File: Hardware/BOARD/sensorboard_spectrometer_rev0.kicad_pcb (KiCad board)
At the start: 2 copper layers, 69.1 x 54.9 mm, 41 parts, among them IC1 CAT4101, U10 ADS1115IDGS, U11 TPS61088RHLT, U3 LILTGO touch, U4 W25Q16JVSS, U5 TLV9001IDCK, U6 MCP9808_MSOP, U7 TRANSLATOR-TXS0108E, U8 DS3231MZ, U9 LT3045xDD

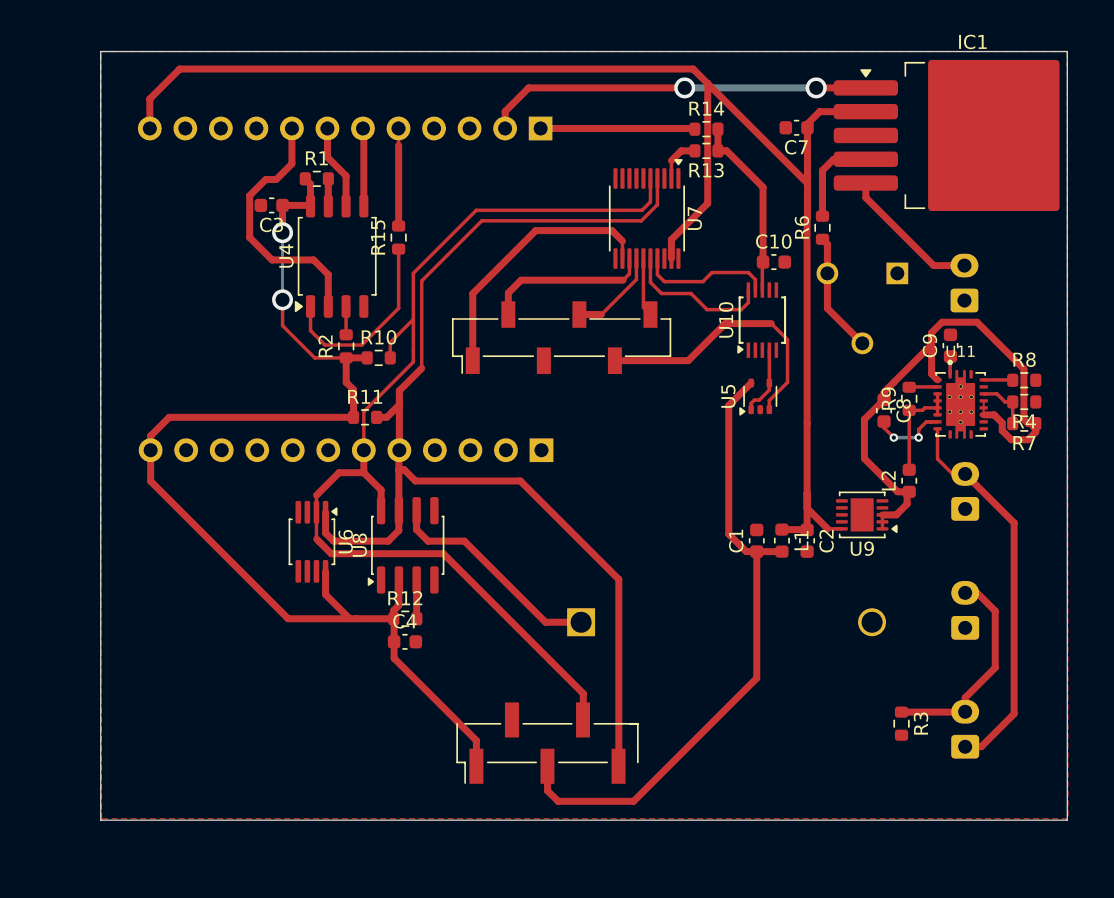
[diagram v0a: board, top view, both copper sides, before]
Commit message: new pcb with the as7331(uv sensor)
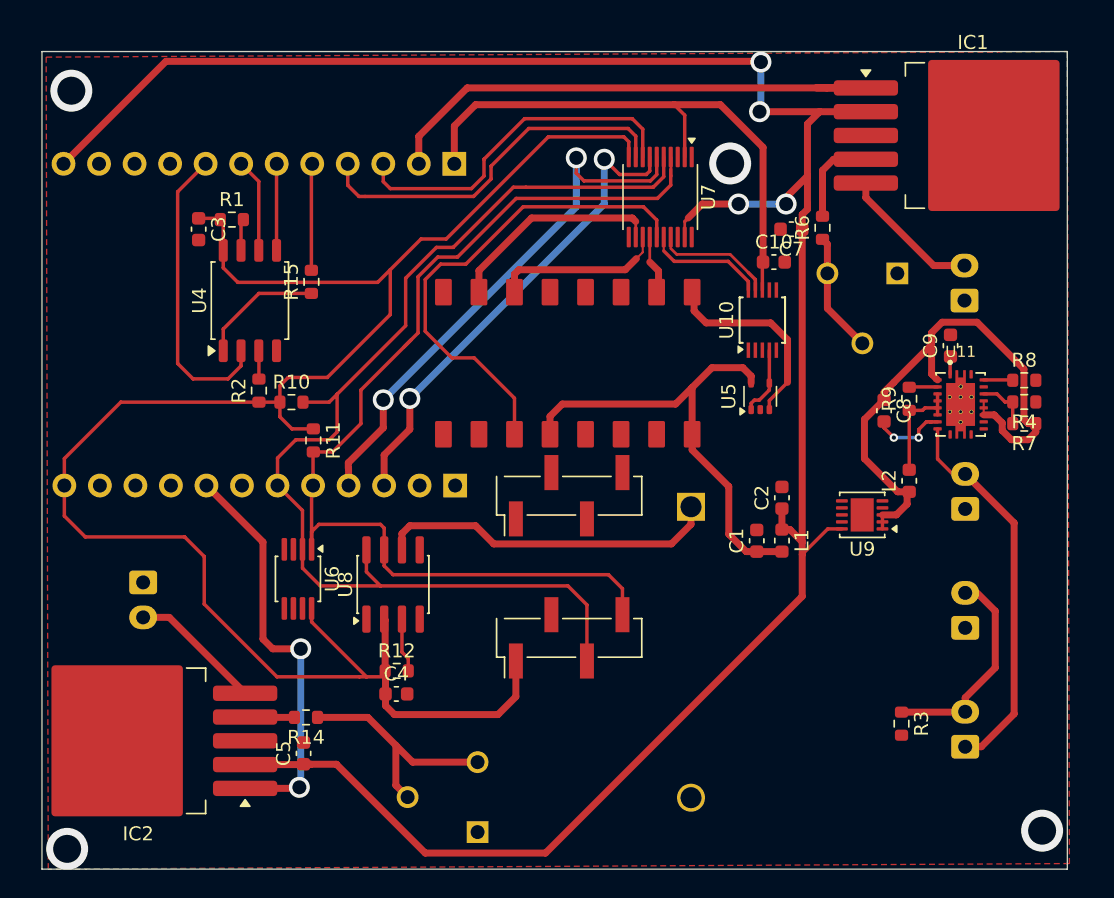
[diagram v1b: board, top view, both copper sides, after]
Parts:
- added C5: 0.1uF, Capacitor_SMD:C_0603_1608Metric, F.Cu at (27.0, 62.3)
- added D2: LED, Connector_JST:JST_EH_S2B-EH_1x02_P2.50mm_Horizontal, B.Cu at (15.5, 50.0)
- added IC2: CAT4101, Package_TO_SOT_SMD:TO-263-5_TabPin6, F.Cu at (15.2, 61.4)
- added U2: ~, mioss:C12880MA_SMD, F.Cu at (42.1, 24.2)
- R13: value 0 -> 5K; footprint Resistor_SMD:R_0603_1608Metric -> Potentiometer_THT:Potentiometer_Runtron_RM-065_Vertical; moved to B.Cu
- R14: value 0 -> 500
- U1: footprint mioss:C12880MA+AS7331 -> mioss:as7331_SMD
- moved R13 51.4 mm to (39.4, 67.9), turned to 90 degrees
- moved R14 50.9 mm to (27.2, 59.7), turned to 180 degrees
- moved U1 21.6 mm to (53.1, 42.2)
- moved BT1 11.4 mm to (54.7, 44.6), turned to -90 degrees
- moved C7 7.26 mm to (61.9, 24.8)
- moved R2 7.00 mm to (23.8, 36.3)
- moved U4 7.00 mm to (23.2, 29.9)
- moved R10 7.00 mm to (26.1, 37.2)
- moved R15 7.00 mm to (27.6, 28.6)
- moved R1 6.74 mm to (21.9, 24.1)
- moved U3 6.67 mm to (-1.04, -19.0)
- moved C3 5.49 mm to (19.5, 24.8), turned to -90 degrees
- moved R11 4.05 mm to (27.7, 39.9), turned to -90 degrees
- moved C4 3.78 mm to (33.6, 58.0)
- moved R12 3.78 mm to (33.7, 56.4)
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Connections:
- R13 pad 1: +3V3 -> GND
- R13 pad 2: Net-(U7-VCCA) -> Net-(R13-E)
- R14 pad 1: Net-(R14-Pad1) -> Net-(R13-E)
- R14 pad 2: +3V3 -> Net-(IC2-RSET)
- U1 pad 1: /V_SPEC -> +3V3
- U1 pad 3: +3V3 -> /I2C_SCL
- U1 pad 4: /I2C_SCL -> /I2C_SDA
- U1 pad 5: /I2C_SDA -> unconnected-(U1-0-Pad5)
- U1 pad 6: /ST_5V -> unconnected-(U1-1-Pad6)
- U1 pad 7: /GAIN_5V -> unconnected-(U1-S-Pad7)
- U1 pad 8: /CLK_5V -> unconnected-(U1-R-Pad8)
- U3 pad 13: Net-(R14-Pad1) -> +3V3
- U3 pad 15: unconnected-(U3-GPIO2-Pad15) -> /GAIN_3V
- U3 pad 16: unconnected-(U3-GPIO3-Pad16) -> /ST_3V
- U3 pad 3: unconnected-(U3-GPIO43-Pad3) -> /EOS_3V
- U3 pad 4: unconnected-(U3-GPIO44-Pad4) -> /CLK_3V
- U3 pad 8: unconnected-(U3-GPIO16-Pad8) -> /PWM_LED_UV
- U5 pad 3: Net-(U1-VIDEO) -> Net-(U2-VIDEO)
- U7 pad 10: 3.3V -> +3V3
- U7 pad 2: Net-(U7-VCCA) -> +3V3
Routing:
- net +3V3: track 97.9 -> 175.5 mm, vias 2 -> 0
- net 5V: track 109.6 -> 168.3 mm, vias 0 -> 4
- net /CLK_3V: track 0.00 -> 38.7 mm, vias 0 -> 2
- net /EOS_3V: track 0.00 -> 34.7 mm, vias 0 -> 2
- net /CLK_5V: track 4.21 -> 34.9 mm
- net /PWM_LED_UV: track 0.00 -> 29.5 mm, vias 0 -> 2
- net /ST_3V: track 0.00 -> 26.7 mm
- net /GAIN_3V: track 0.00 -> 25.1 mm
- net Net-(U1-VIDEO): track 19.2 -> 0.00 mm
- net Net-(R13-E): track 0.00 -> 16.8 mm
- net Net-(U2-VIDEO): track 0.00 -> 14.1 mm
- net /V_SPEC: track 45.6 -> 33.7 mm
- net /PWM_LED: track 27.7 -> 39.0 mm, vias 2 -> 0
- net Net-(R14-Pad1): track 11.0 -> 0.00 mm
- net Net-(D2-A): track 0.00 -> 9.54 mm
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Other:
- board size 69.1 x 54.9 mm -> 73.3 x 58.4 mm

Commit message: before maked
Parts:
- removed C5, C7: 0.1uF, Capacitor_SMD:C_0603_1608Metric
- removed IC1, IC2: CAT4101, Package_TO_SOT_SMD:TO-263-5_TabPin6
- added R16: 0, Resistor_SMD:R_0603_1608Metric, F.Cu at (59.9, 23.0)
- added REF**: R_0603_1608Metric, Resistor_SMD:R_0603_1608Metric, F.Cu at (27.5, 56.8)
- added U1: TXS0108EPW, Package_SO:TSSOP-20_4.4x6.5mm_P0.65mm, F.Cu at (52.0, 22.3)
- added U12: ~, Package_SO:PowerIntegrations_SO-8, F.Cu at (15.9, 64.2)
- R13: value 5K -> 0; footprint Potentiometer_THT:Potentiometer_Runtron_RM-065_Vertical -> Resistor_SMD:R_0603_1608Metric; moved to F.Cu
- R14: value 500 -> 0
- R5: value 5K -> 768; footprint Potentiometer_THT:Potentiometer_Runtron_RM-065_Vertical -> Resistor_SMD:R_0603_1608Metric; moved to F.Cu
- R6: value 500 -> 768
- U7: value TRANSLATOR-TXS0108E -> ~; footprint Package_SO:TSSOP-20_4.4x5mm_P0.5mm -> Package_SO:PowerIntegrations_SO-8
- moved R5 58.7 mm to (22.7, 63.5), turned to -90 degrees
- moved R14 47.3 mm to (70.2, 39.9)
- moved R13 26.9 mm to (19.9, 49.5), turned to 0 degrees
- moved U7 22.8 mm to (74.9, 18.2), turned to 180 degrees
- moved R6 4.86 mm to (68.6, 22.8), turned to 180 degrees
- moved C3 2.57 mm to (17.0, 24.1), turned to 180 degrees
- moved D1 1.75 mm to (74.4, 28.1)
- moved R2 0.51 mm to (23.3, 36.3)
- renumbered U1 to AS7331
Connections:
- C8 pad 2: Net-(U11-BOOT) -> Net-(C8-Pad2)
- D1 pad 1: GND -> Net-(D1-K)
- D1 pad 2: Net-(D1-A) -> 5V
- D2 pad 1: GND -> Net-(D2-K)
- D2 pad 2: Net-(D2-A) -> 5V
- R13 pad 1: GND -> /PWM_LED_UV
- R13 pad 2: Net-(R13-E) -> Net-(U3-GPIO16)
- R14 pad 1: Net-(R13-E) -> Net-(U11-BOOT)
- R14 pad 2: Net-(IC2-RSET) -> Net-(C8-Pad2)
- R5 pad 1: GND -> Net-(U12-RESET)
- R5 pad 2: Net-(R5-E) -> GND
- R6 pad 1: Net-(R5-E) -> Net-(U7-GND)
- R6 pad 2: Net-(IC1-RSET) -> GND
- U3 pad 8: /PWM_LED_UV -> Net-(U3-GPIO16)
- U7 pad 1: unconnected-(U7-A1-Pad1) -> Net-(D1-K)
- U7 pad 2: +3V3 -> Net-(D1-K)
- U7 pad 4: /I2C_SDA -> unconnected-(U7-led4-Pad4)
- U7 pad 5: /I2C_SCL -> Net-(U7-GND)
- U7 pad 6: /CLK_3V -> 5V
- U7 pad 7: /EOS_3V -> /PWM_LED
- U7 pad 8: /GAIN_3V -> GND
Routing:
- net GND: track 0.00 -> 29.2 mm
- net +3V3: track 175.5 -> 147.8 mm
- net 5V: track 168.3 -> 195.0 mm, vias 4 -> 2
- net Net-(R13-E): track 16.8 -> 0.00 mm
- net Net-(D2-K): track 0.00 -> 15.4 mm
- net Net-(U7-GND): track 0.00 -> 13.2 mm
- net Net-(D1-K): track 0.00 -> 11.6 mm
- net Net-(D1-A): track 10.1 -> 0.00 mm
- net Net-(D2-A): track 9.54 -> 0.00 mm
- net Net-(R5-E): track 8.62 -> 0.00 mm
- net Net-(IC1-RSET): track 6.71 -> 0.00 mm
- net Net-(U3-GPIO16): track 0.00 -> 6.64 mm
- net Net-(U1-VCCB): track 0.00 -> 6.40 mm
- net /PWM_LED_UV: track 29.5 -> 34.6 mm, vias 2 -> 0
- net Net-(U12-RESET): track 0.00 -> 4.27 mm
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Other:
- board size 73.3 x 58.4 mm -> 74.2 x 57.2 mm

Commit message: alex suggest changes
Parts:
- removed REF**: R_0603_1608Metric, Resistor_SMD:R_0603_1608Metric
- C3: footprint Capacitor_SMD:C_0603_1608Metric -> Capacitor_SMD:C_1206_3216Metric
- R11, R13, R15, R16, R2: footprint Resistor_SMD:R_0603_1608Metric -> Resistor_SMD:R_1206_3216Metric
- moved R10 2.45 mm to (28.5, 36.5)
- moved R2 1.10 mm to (23.8, 37.3)
- moved R15 0.53 mm to (28.1, 28.6)
- moved R11 0.28 mm to (27.7, 39.6)
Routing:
- net GND: track 29.2 -> 19.6 mm
- net +3V3: track 147.8 -> 143.8 mm
- net 5V: track 195.0 -> 198.8 mm
- net /I2C_SCL: track 83.1 -> 82.1 mm
- net Net-(U1-VCCB): track 6.40 -> 5.76 mm
- net +5.5V: track 42.4 -> 41.8 mm
- net Net-(U11-FSW): track 2.09 -> 1.53 mm
- net /EOS_3V: vias 3 -> 2
- net /CLK_3V: vias 2 -> 1

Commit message: not shot resistors
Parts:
- added REF**: R_1206_3216Metric_Pad1.30x1.75mm_HandSolder, Resistor_SMD:R_1206_3216Metric_Pad1.30x1.75mm_HandSolder, F.Cu at (65.3, 29.7)
- added REF**: R_1206_3216Metric_Pad1.30x1.75mm_HandSolder, Resistor_SMD:R_1206_3216Metric_Pad1.30x1.75mm_HandSolder, F.Cu at (26.9, 56.7)
- moved R6 6.60 mm to (68.4, 16.2)
- moved C9 0.86 mm to (74.0, 33.5), turned to 0 degrees
- moved R14 0.12 mm to (70.3, 39.9)
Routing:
- net Net-(U7-GND): track 13.2 -> 3.00 mm
- net /PWM_LED: track 42.9 -> 52.2 mm
- net GND: track 19.6 -> 28.8 mm
- net 5V: track 198.8 -> 208.0 mm
- net +5.5V: track 41.8 -> 49.1 mm
- net Net-(C8-Pad2): track 1.44 -> 2.21 mm
- net Net-(U11-FSW): track 1.53 -> 2.09 mm
- net /CLK_3V: vias 1 -> 2
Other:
- board size 74.2 x 57.2 mm -> 75.4 x 58.5 mm

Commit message: alex suggest changes again...
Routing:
- net GND: track 28.8 -> 39.9 mm, vias 0 -> 10
- net +3V3: track 143.8 -> 144.6 mm
- added copper zone on B.Cu, net GND
